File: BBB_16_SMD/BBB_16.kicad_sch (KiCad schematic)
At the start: 45 parts, among them J17 Power In Left, J18 Power In Right, J19 GPIO, J23 VIN Voltage, J24 Expansion Header, J25 RTC Conn, J26 OLED, J27 Aux Pwr, J28 VIN Select, Q1 DMP3056L, SW1 Left BTN, SW2 Up BTN, SW3 Down BTN, SW4 Right BTN, SW5 PWR BTN, U2 LM7805, U6 24L256

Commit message: finished routing
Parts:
- U2: footprint Package_TO_SOT_THT:TO-220-3_Vertical -> OKI-78SR-5:SIP-3_P2.54mm_OKI-78SR-5_1.5-W36-C
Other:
- title: BBB 16 -> BBB 16 SMD
- moved on the sheet: D4, J19, J25, R3

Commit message: added boms
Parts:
- C1: LCSC (none) -> C88784
- C6: Digi-Key_PN 478-7336-1-ND -> 1276-1935-2-ND; LCSC (none) -> C14663; MPN SR215C104KARTR1 -> CL10B104KB8NNWC
- D4: Digi-Key_PN 160-1423-1-ND -> 160-1436-2-ND; LCSC C2297 -> C2286; MPN LTST-C171GKT -> LTST-C190KRKT
- D5, D6: Digi-Key_PN 754-1217-ND -> 160-1436-2-ND; LCSC (none) -> C2286; MPN WP3A8GD -> LTST-C190KRKT
- F17, F18: LCSC (none) -> C492610
- J17, J18: LCSC (none) -> C707421
- J19: LCSC (none) -> C144395
- J23, J28: LCSC (none) -> C49257
- J24: LCSC (none) -> C221083
- J25: LCSC (none) -> C358687
- J26: LCSC (none) -> C225501
- J27: LCSC (none) -> C69811
- R10, R13: Digi-Key_PN MFR-25FBF52-680R-ND -> 311-680HRCT-ND; LCSC (none) -> C23228; MPN MFR-25FBF52-680R -> RC0603FR-07680RL
- R11, R8: Digi-Key_PN CF14JT100RCT-ND -> RMCF0603FT100RCT-ND; LCSC (none) -> C22775; MPN CF14JT100R -> RMCF0603FT100R
- R12, R9: Digi-Key_PN RNF14FTD10K0CT-ND -> 311-10.0KHRCT-ND; LCSC (none) -> C25804; MPN RNF14FTD10K0 -> RC0603FR-0710KL
- R14: Digi-Key_PN 311-100KCRCT-ND -> YAG1235CT-ND; LCSC C17407 -> C25803; MPN RC0805FR-07100KL -> RT0603BRD07100KL
- R3: Digi-Key_PN CF14JT120RCT-ND -> A129677CT-ND; LCSC (none) -> C22787; MPN CF14JT120R -> CRGCQ0603F120R
- R4, R5: Digi-Key_PN CF14JT1K00CT-ND -> 311-1.00KHRTR-ND; LCSC (none) -> C21190; MPN CF14JT1K00 -> RC0603FR-071KL
- R6, R7: Digi-Key_PN CF14JT4K70CT-ND -> 311-4.7KGRCT-ND; LCSC (none) -> C23162; MPN CF14JT4K70 -> RC0603JR-074K7L
- SW1, SW2, SW3, SW4, SW5: Digi-Key_PN 450-1650-ND -> CKN9088CT-ND; LCSC (none) -> C127509; MPN 1825910-6 -> PTS645SL50SMTR92 LFS
- U6: Digi-Key_PN 1219-1052-ND -> 24LC256T-I/MSCT-ND; LCSC (none) -> C6482; MPN FT24C256A-UDR-B -> 24LC256T-I/MS

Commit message: ~Create some new custom footprints ~Update some JLC PN's ~Updated some 3D model paths
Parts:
- J26: footprint OLED-SSD1306-128X64-I2C:OLED-SSD1306-128X64-I2C-THT -> Scotts:OLED-SSD1306-128X64-I2C-THT_2HOLE
- U2: footprint OKI-78SR-5:SIP-3_P2.54mm_OKI-78SR-5_1.5-W36-C -> Scotts:OKI-78SR
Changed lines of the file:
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@@
     (property "Reference" "U2" (id 0) (at 223.266 33.8582 0))
     (property "Value" "LM7805" (id 1) (at 223.266 36.1696 0))
-    (property "Footprint" "OKI-78SR-5:SIP-3_P2.54mm_OKI-78SR-5_1.5-W36-C" (id 2) (at 223.266 34.29 0)
+    (property "Footprint" "Scotts:OKI-78SR" (id 2) (at 223.266 34.29 0)
       (effects (font (size 1.27 1.27) italic) hide)
     )
@@
     (property "Reference" "J26" (id 0) (at 33.2232 28.829 0))
     (property "Value" "OLED" (id 1) (at 33.2232 31.1404 0))
-    (property "Footprint" "OLED-SSD1306-128X64-I2C:OLED-SSD1306-128X64-I2C-THT" (id 2) (at 30.48 36.068 0)
+    (property "Footprint" "Scotts:OLED-SSD1306-128X64-I2C-THT_2HOLE" (id 2) (at 30.48 36.068 0)
       (effects (font (size 1.27 1.27)) hide)
     )
@@
     )
     (path "/00000000-0000-0000-0000-00005d551e96"
-      (reference "J26") (unit 1) (value "OLED") (footprint "OLED-SSD1306-128X64-I2C:OLED-SSD1306-128X64-I2C-THT")
+      (reference "J26") (unit 1) (value "OLED") (footprint "Scotts:OLED-SSD1306-128X64-I2C-THT_2HOLE")
     )
     (path "/00000000-0000-0000-0000-0000617ff4f3"
@@
     )
     (path "/00000000-0000-0000-0000-00005d413c25/00000000-0000-0000-0000-00005e1aa21a"
-      (reference "U1") (unit 1) (value "BEAGLEBONEBLACK") (footprint "beagleboneblack:BEAGLEBONEBLACK")
+      (reference "U1") (unit 1) (value "BEAGLEBONEBLACK") (footprint "Scotts:BEAGLEBONEBLACK")
     )
     (path "/00000000-0000-0000-0000-00005d413c25/00000000-0000-0000-0000-00005e1af788"
-      (reference "U1") (unit 2) (value "BEAGLEBONEBLACK") (footprint "beagleboneblack:BEAGLEBONEBLACK")
+      (reference "U1") (unit 2) (value "BEAGLEBONEBLACK") (footprint "Scotts:BEAGLEBONEBLACK")
     )
     (path "/00000000-0000-0000-0000-00005d413c25/00000000-0000-0000-0000-00005e1b579b"
-      (reference "U1") (unit 3) (value "BEAGLEBONEBLACK") (footprint "beagleboneblack:BEAGLEBONEBLACK")
+      (reference "U1") (unit 3) (value "BEAGLEBONEBLACK") (footprint "Scotts:BEAGLEBONEBLACK")
     )
     (path "/00000000-0000-0000-0000-00005d413c25/00000000-0000-0000-0000-00005e1b9a69"
-      (reference "U1") (unit 4) (value "BEAGLEBONEBLACK") (footprint "beagleboneblack:BEAGLEBONEBLACK")
+      (reference "U1") (unit 4) (value "BEAGLEBONEBLACK") (footprint "Scotts:BEAGLEBONEBLACK")
     )
     (path "/00000000-0000-0000-0000-00005cecc219"
-      (reference "U2") (unit 1) (value "LM7805") (footprint "OKI-78SR-5:SIP-3_P2.54mm_OKI-78SR-5_1.5-W36-C")
+      (reference "U2") (unit 1) (value "LM7805") (footprint "Scotts:OKI-78SR")
     )
     (path "/00000000-0000-0000-0000-00005d469293/00000000-0000-0000-0000-00005d4cfc0f"

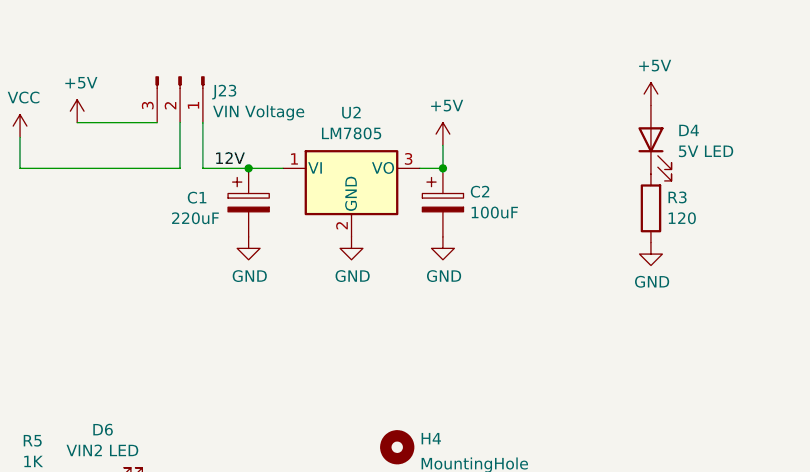
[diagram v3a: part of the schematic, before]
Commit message: added universal 5V Reg
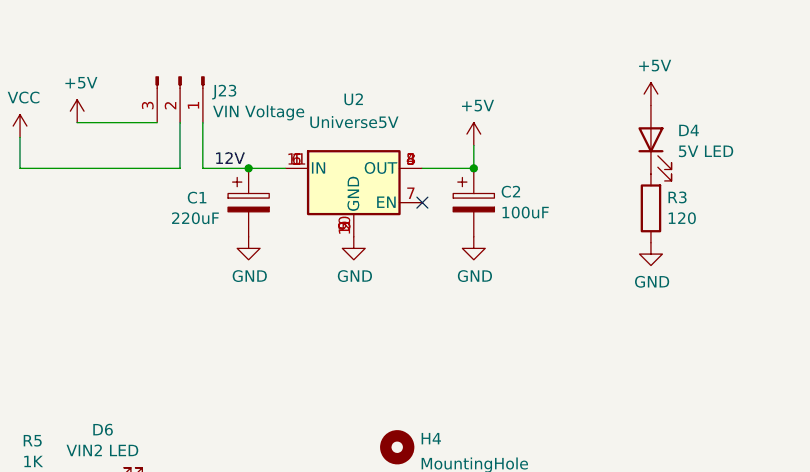
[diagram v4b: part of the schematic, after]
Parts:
- removed U2: LM7805, Scotts:OKI-78SR, symbol Regulator_Linear:LM7805_TO220
- added U2: Universe5V, Scotts:Universal_5V_Horizontal, symbol Scotts:Universe5V
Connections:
- net +5V: now also U2.3 (OUT), U2.4 (OUT), U2.8 (OUT)
- net 12V: now also U2.1 (IN), U2.11 (IN), U2.6 (IN)
- net GND: now also U2.10 (GND), U2.2 (GND), U2.5 (GND), U2.9 (GND)
- no-connect marks 1 -> 2
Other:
- moved on the sheet: C2
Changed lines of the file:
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@@
   (title_block
     (title "BBB 16 SMD")
-    (date "2022-02-11")
-    (rev "v2")
+    (date "2022-08-14")
+    (rev "v3")
     (company "Scott Hanson")
   )
@@
   (junction (at 169.418 34.798) (diameter 0) (color 0 0 0 0)
   )
-  (junction (at 233.426 40.005) (diameter 0) (color 0 0 0 0)
+  (junction (at 236.855 40.005) (diameter 0) (color 0 0 0 0)
   )
   (no_connect (at 81.28 29.21))
+  (no_connect (at 231.14 43.815))
   (wire (pts (xy 210.566 147.32) (xy 212.344 147.32))
     (stroke (width 0) (type default) (color 0 0 0 0))
@@
     (stroke (width 0) (type default) (color 0 0 0 0))
   )
-  (wire (pts (xy 215.646 40.005) (xy 211.836 40.005))
+  (wire (pts (xy 211.836 40.005) (xy 215.9 40.005))
     (stroke (width 0) (type default) (color 0 0 0 0))
   )
@@
     (stroke (width 0) (type default) (color 0 0 0 0))
   )
+  (wire (pts (xy 231.14 40.005) (xy 236.855 40.005))
+    (stroke (width 0) (type default) (color 0 0 0 0))
+  )
   (wire (pts (xy 148.717 32.766) (xy 148.717 34.798))
     (stroke (width 0) (type default) (color 0 0 0 0))
@@
     (stroke (width 0) (type default) (color 0 0 0 0))
   )
-  (wire (pts (xy 230.886 40.005) (xy 233.426 40.005))
-    (stroke (width 0) (type default) (color 0 0 0 0))
-  )
   (wire (pts (xy 190.246 149.86) (xy 190.246 152.4))
     (stroke (width 0) (type default) (color 0 0 0 0))
   )
-  (wire (pts (xy 233.426 40.005) (xy 233.426 37.465))
+  (wire (pts (xy 236.855 40.005) (xy 236.855 37.465))
     (stroke (width 0) (type default) (color 0 0 0 0))
   )
@@
     )
   )
-  (symbol (lib_id "Regulator_Linear:LM7805_TO220") (at 223.266 40.005 0) (unit 1)
-    (in_bom yes) (on_board yes)
-    (property "Reference" "U2" (id 0) (at 223.266 33.8582 0))
-    (property "Value" "LM7805" (id 1) (at 223.266 36.1696 0))
-    (property "Footprint" "Scotts:OKI-78SR" (id 2) (at 223.266 34.29 0)
-      (effects (font (size 1.27 1.27) italic) hide)
-    )
-    (property "Datasheet" "http://www.fairchildsemi.com/ds/LM/LM7805.pdf" (id 3) (at 223.266 41.275 0)
-      (effects (font (size 1.27 1.27)) hide)
-    )
-    (property "Digi-Key_PN" "811-2196-5-ND" (id 4) (at -7.874 84.709 0)
-      (effects (font (size 1.27 1.27)) hide)
-    )
-    (property "MPN" "OKI-78SR-5/1.5-W36-C" (id 5) (at -7.874 84.709 0)
-      (effects (font (size 1.27 1.27)) hide)
-    )
-    (pin "1")
-    (pin "2")
-    (pin "3")
-  )
-  (symbol (lib_id "BBB_16-rescue:CP-Device") (at 233.426 43.815 0) (unit 1)
-    (in_bom yes) (on_board yes)
-    (property "Reference" "C2" (id 0) (at 236.4232 42.6466 0)
-      (effects (font (size 1.27 1.27)) (justify left))
-    )
-    (property "Value" "100uF" (id 1) (at 236.4232 44.958 0)
-      (effects (font (size 1.27 1.27)) (justify left))
-    )
-    (property "Footprint" "Capacitor_SMD:CP_Elec_6.3x5.4_Nichicon" (id 2) (at 234.3912 47.625 0)
-      (effects (font (size 1.27 1.27)) hide)
-    )
-    (property "Datasheet" "~" (id 3) (at 233.426 43.815 0)
-      (effects (font (size 1.27 1.27)) hide)
-    )
-    (property "Digi-Key_PN" "493-2105-1-ND" (id 4) (at -9.652 92.329 0)
-      (effects (font (size 1.27 1.27)) hide)
-    )
-    (property "MPN" "UWX1C101MCL1GB" (id 5) (at -9.652 92.329 0)
-      (effects (font (size 1.27 1.27)) hide)
-    )
-    (property "LCSC" "C134723" (id 6) (at 233.426 43.815 0)
+  (symbol (lib_id "BBB_16-rescue:CP-Device") (at 236.855 43.815 0) (unit 1)
+    (in_bom yes) (on_board yes)
+    (property "Reference" "C2" (id 0) (at 239.8522 42.6466 0)
+      (effects (font (size 1.27 1.27)) (justify left))
+    )
+    (property "Value" "100uF" (id 1) (at 239.8522 44.958 0)
+      (effects (font (size 1.27 1.27)) (justify left))
+    )
+    (property "Footprint" "Capacitor_SMD:CP_Elec_6.3x5.4_Nichicon" (id 2) (at 237.8202 47.625 0)
+      (effects (font (size 1.27 1.27)) hide)
+    )
+    (property "Datasheet" "~" (id 3) (at 236.855 43.815 0)
+      (effects (font (size 1.27 1.27)) hide)
+    )
+    (property "Digi-Key_PN" "493-2105-1-ND" (id 4) (at -6.223 92.329 0)
+      (effects (font (size 1.27 1.27)) hide)
+    )
+    (property "MPN" "UWX1C101MCL1GB" (id 5) (at -6.223 92.329 0)
+      (effects (font (size 1.27 1.27)) hide)
+    )
+    (property "LCSC" "C134723" (id 6) (at 236.855 43.815 0)
       (effects (font (size 1.27 1.27)) hide)
     )
@@
     (pin "1")
   )
-  (symbol (lib_id "power:GND") (at 223.266 47.625 0) (unit 1)
-    (in_bom yes) (on_board yes)
-    (property "Reference" "#PWR0113" (id 0) (at 223.266 53.975 0)
-      (effects (font (size 1.27 1.27)) hide)
-    )
-    (property "Value" "GND" (id 1) (at 223.393 52.0192 0))
-    (property "Footprint" "" (id 2) (at 223.266 47.625 0)
-      (effects (font (size 1.27 1.27)) hide)
-    )
-    (property "Datasheet" "" (id 3) (at 223.266 47.625 0)
-      (effects (font (size 1.27 1.27)) hide)
-    )
-    (pin "1")
-  )
-  (symbol (lib_id "power:GND") (at 233.426 47.625 0) (unit 1)
-    (in_bom yes) (on_board yes)
-    (property "Reference" "#PWR0114" (id 0) (at 233.426 53.975 0)
-      (effects (font (size 1.27 1.27)) hide)
-    )
-    (property "Value" "GND" (id 1) (at 233.553 52.0192 0))
-    (property "Footprint" "" (id 2) (at 233.426 47.625 0)
-      (effects (font (size 1.27 1.27)) hide)
-    )
-    (property "Datasheet" "" (id 3) (at 233.426 47.625 0)
+  (symbol (lib_id "power:GND") (at 223.52 47.625 0) (unit 1)
+    (in_bom yes) (on_board yes)
+    (property "Reference" "#PWR0113" (id 0) (at 223.52 53.975 0)
+      (effects (font (size 1.27 1.27)) hide)
+    )
+    (property "Value" "GND" (id 1) (at 223.647 52.0192 0))
+    (property "Footprint" "" (id 2) (at 223.52 47.625 0)
+      (effects (font (size 1.27 1.27)) hide)
+    )
+    (property "Datasheet" "" (id 3) (at 223.52 47.625 0)
+      (effects (font (size 1.27 1.27)) hide)
+    )
+    (pin "1")
+  )
+  (symbol (lib_id "power:GND") (at 236.855 47.625 0) (unit 1)
+    (in_bom yes) (on_board yes)
+    (property "Reference" "#PWR0114" (id 0) (at 236.855 53.975 0)
+      (effects (font (size 1.27 1.27)) hide)
+    )
+    (property "Value" "GND" (id 1) (at 236.982 52.0192 0))
+    (property "Footprint" "" (id 2) (at 236.855 47.625 0)
+      (effects (font (size 1.27 1.27)) hide)
+    )
+    (property "Datasheet" "" (id 3) (at 236.855 47.625 0)
       (effects (font (size 1.27 1.27)) hide)
     )
@@
     (pin "1")
   )
-  (symbol (lib_id "power:+5V") (at 233.426 37.465 0) (unit 1)
-    (in_bom yes) (on_board yes)
-    (property "Reference" "#PWR0116" (id 0) (at 233.426 41.275 0)
-      (effects (font (size 1.27 1.27)) hide)
-    )
-    (property "Value" "+5V" (id 1) (at 233.807 33.0708 0))
-    (property "Footprint" "" (id 2) (at 233.426 37.465 0)
-      (effects (font (size 1.27 1.27)) hide)
-    )
-    (property "Datasheet" "" (id 3) (at 233.426 37.465 0)
+  (symbol (lib_id "power:+5V") (at 236.855 37.465 0) (unit 1)
+    (in_bom yes) (on_board yes)
+    (property "Reference" "#PWR0116" (id 0) (at 236.855 41.275 0)
+      (effects (font (size 1.27 1.27)) hide)
+    )
+    (property "Value" "+5V" (id 1) (at 237.236 33.0708 0))
+    (property "Footprint" "" (id 2) (at 236.855 37.465 0)
+      (effects (font (size 1.27 1.27)) hide)
+    )
+    (property "Datasheet" "" (id 3) (at 236.855 37.465 0)
       (effects (font (size 1.27 1.27)) hide)
     )
@@
     )
   )
+  (symbol (lib_id "Scotts:Universe5V") (at 223.52 40.005 0) (unit 1)
+    (in_bom yes) (on_board yes) (fields_autoplaced)
+    (property "Reference" "U2" (id 0) (at 223.52 32.385 0))
+    (property "Value" "Universe5V" (id 1) (at 223.52 34.925 0))
+    (property "Footprint" "Scotts:Universal_5V_Horizontal" (id 2) (at 224.155 43.815 0)
+      (effects (font (size 1.27 1.27) italic) (justify left) hide)
+    )
+    (property "Datasheet" "" (id 3) (at 223.52 41.275 0)
+      (effects (font (size 1.27 1.27)) hide)
+    )
+    (pin "10")
+    (pin "11")
+    (pin "4")
+    (pin "5")
+    (pin "6")
+    (pin "7")
+    (pin "8")
+    (pin "9")
+    (pin "1")
+    (pin "2")
+    (pin "3")
+  )
   (symbol (lib_id "PB_16-rescue:3544-2-Keystone_Fuse") (at 127.381 34.798 0) (unit 1)
     (in_bom yes) (on_board yes)
@@
       (reference "U1") (unit 4) (value "BEAGLEBONEBLACK") (footprint "Scotts:BEAGLEBONEBLACK")
     )
-    (path "/00000000-0000-0000-0000-00005cecc219"
-      (reference "U2") (unit 1) (value "LM7805") (footprint "Scotts:OKI-78SR")
+    (path "/c2881f4f-a886-4d1e-a891-4bc584fa6a95"
+      (reference "U2") (unit 1) (value "Universe5V") (footprint "Scotts:Universal_5V_Horizontal")
     )
     (path "/00000000-0000-0000-0000-00005d469293/00000000-0000-0000-0000-00005d4cfc0f"
